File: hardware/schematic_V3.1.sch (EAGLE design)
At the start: 22 parts, among them J1 POWER_JACKPTH, J2 ARDUINONANO, J3 ICSP, J4 ICSP, J5 2.54mm, J6 2.54mm, J7 2.54mm, J8 2.54mm, J9 2.54mm, U1 L9110S_DRIVER

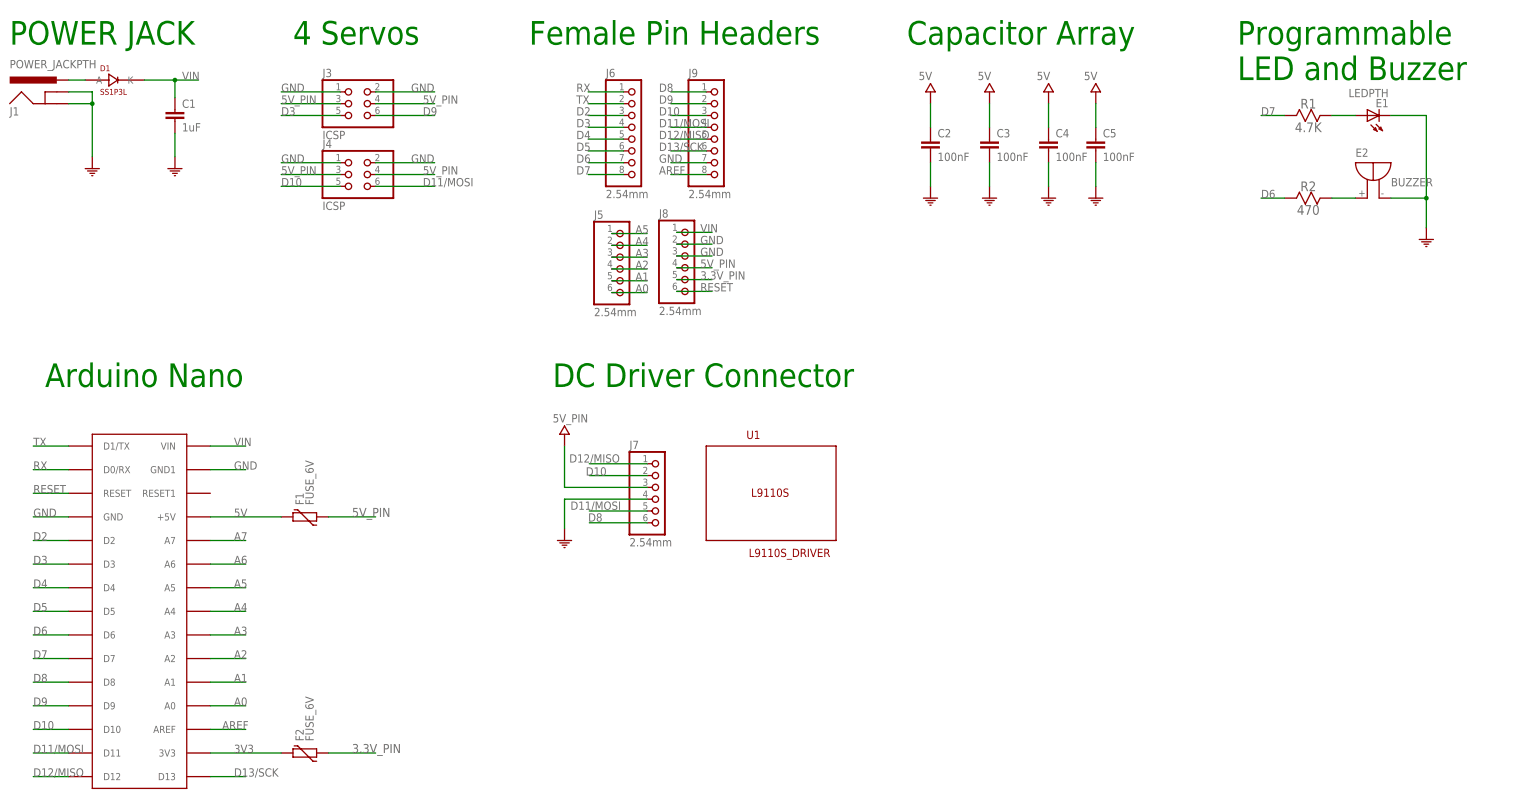
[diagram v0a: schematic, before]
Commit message: Finished routing and change the logo
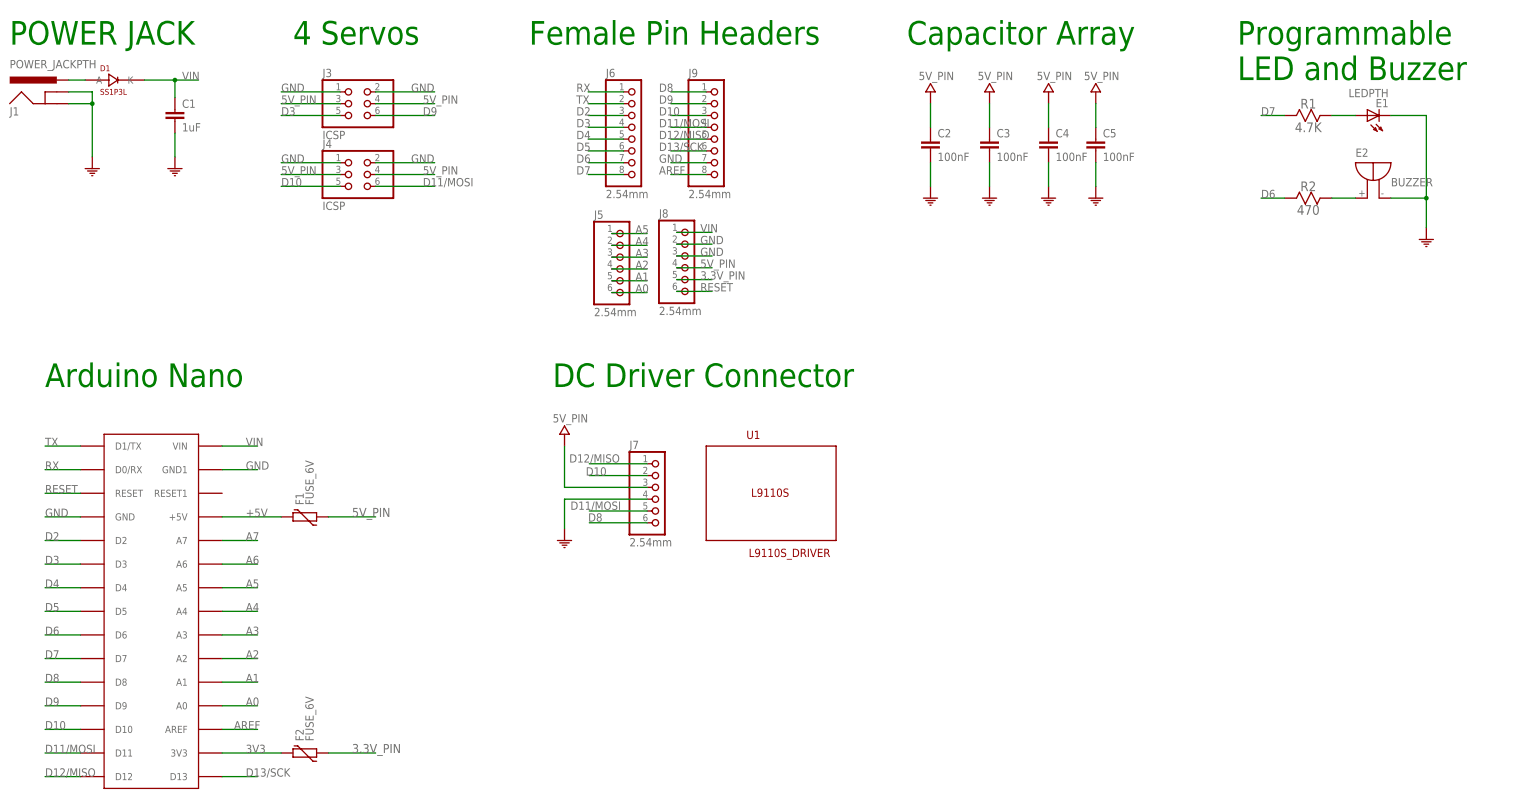
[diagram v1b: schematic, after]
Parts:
- removed J2: ARDUINONANO, barnabas_noggin_V4:ARDUINONANO
- added U$1: ARDUINONANO, barnabas_noggin_V4:ARDUINONANO
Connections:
- removed net 5V: C2.1, C3.1, C4.1, C5.1, F1.2, J2.+5V
- new net +5V: F1.2, U$1.+5V
- net 3V3: now also U$1.3V3; no longer J2.3V3
- net 5V_PIN: now also C2.1, C3.1, C4.1, C5.1
- net A0: now also U$1.A0; no longer J2.A0
- net A1: now also U$1.A1; no longer J2.A1
- net A2: now also U$1.A2; no longer J2.A2
- net A3: now also U$1.A3; no longer J2.A3
- net A4: now also U$1.A4; no longer J2.A4
- net A5: now also U$1.A5; no longer J2.A5
- net A6: now also U$1.A6; no longer J2.A6
- net A7: now also U$1.A7; no longer J2.A7
- net AREF: now also U$1.AREF; no longer J2.AREF
- net D10: now also U$1.D10; no longer J2.D10
- net D11/MOSI: now also U$1.D11; no longer J2.D11
- net D12/MISO: now also U$1.D12; no longer J2.D12
- net D13/SCK: now also U$1.D13; no longer J2.D13
- net D2: now also U$1.D2; no longer J2.D2
- net D3: now also U$1.D3; no longer J2.D3
- net D4: now also U$1.D4; no longer J2.D4
- net D5: now also U$1.D5; no longer J2.D5
- net D6: now also U$1.D6; no longer J2.D6
- net D7: now also U$1.D7; no longer J2.D7
- net D8: now also U$1.D8; no longer J2.D8
- net D9: now also U$1.D9; no longer J2.D9
- net GND: now also U$1.GND, U$1.GND1; no longer J2.GND, J2.GND1
- net RESET: now also U$1.RESET; no longer J2.RESET
- net RX: now also U$1.D0/RX; no longer J2.D0/RX
- net TX: now also U$1.D1/TX; no longer J2.D1/TX
- net VIN: now also U$1.VIN; no longer J2.VIN

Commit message: Moved the logo and generated BOM
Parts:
- F1, F2: PARTNO (none) -> MF-FSMF050X-2
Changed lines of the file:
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@@
 <part name="SYMBLE3" library="barnabas_noggin_V4" deviceset="5V_PIN" device=""/>
 <part name="SYMBLE4" library="barnabas_noggin_V4" deviceset="GND" device=""/>
-<part name="F1" library="barnabas_noggin_V4" deviceset="FUSE_6V" device=""/>
-<part name="F2" library="barnabas_noggin_V4" deviceset="FUSE_6V" device=""/>
+<part name="F1" library="barnabas_noggin_V4" deviceset="FUSE_6V" device="">
+<attribute name="PARTNO" value="MF-FSMF050X-2"/>
+</part>
+<part name="F2" library="barnabas_noggin_V4" deviceset="FUSE_6V" device="">
+<attribute name="PARTNO" value="MF-FSMF050X-2"/>
+</part>
 <part name="U$1" library="barnabas_noggin_V4" deviceset="ARDUINONANO" device=""/>
 <part name="SYMBLE5" library="barnabas_noggin_V4" deviceset="5V_PIN" device=""/>
@@
 <instance part="SYMBLE3" gate="G$1" x="106.68" y="40.64"/>
 <instance part="SYMBLE4" gate="G$1" x="106.68" y="17.78"/>
-<instance part="F1" gate="G$1" x="50.8" y="22.86" rot="R90"/>
-<instance part="F2" gate="G$1" x="50.8" y="-27.94" rot="R90"/>
+<instance part="F1" gate="G$1" x="50.8" y="22.86" rot="R90">
+<attribute name="PARTNO" x="50.8" y="22.86" size="1.778" layer="96" rot="R90" display="off"/>
+</instance>
+<instance part="F2" gate="G$1" x="50.8" y="-27.94" rot="R90">
+<attribute name="PARTNO" x="50.8" y="-27.94" size="1.778" layer="96" rot="R90" display="off"/>
+</instance>
 <instance part="U$1" gate="G$1" x="7.62" y="40.64"/>
 <instance part="SYMBLE5" gate="G$1" x="185.42" y="114.3"/>

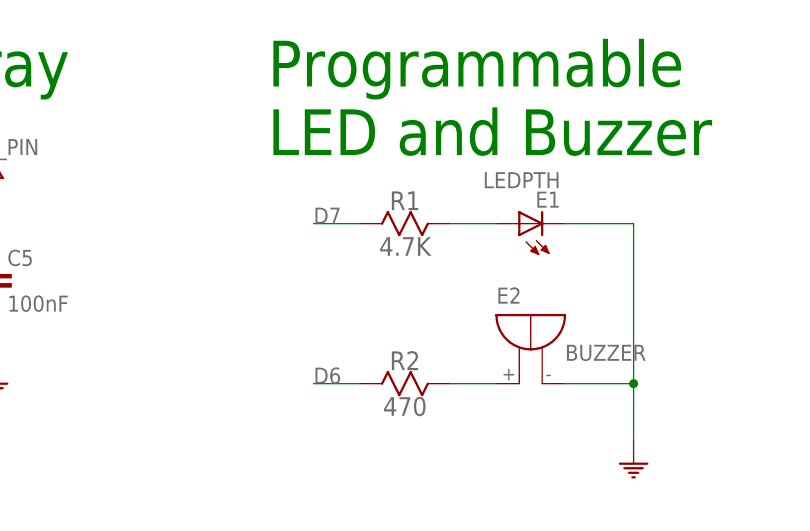
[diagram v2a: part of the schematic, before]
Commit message: change 4.7K resistor to 470 resistor
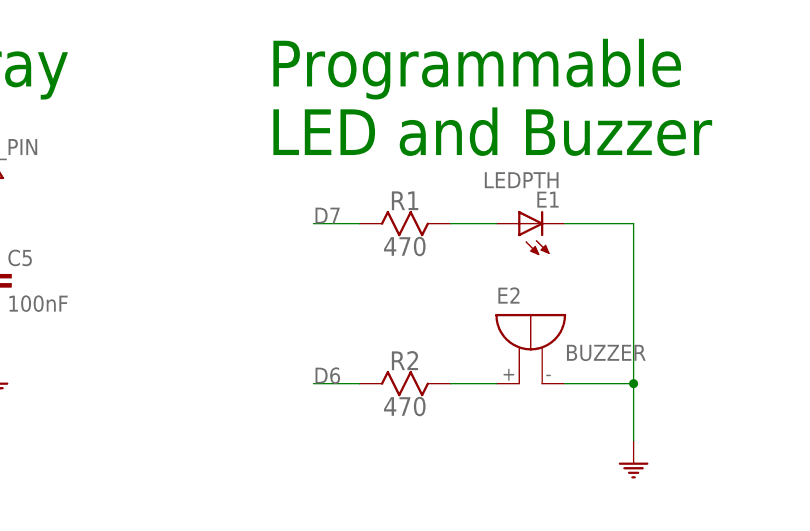
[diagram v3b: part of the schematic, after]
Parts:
- R1: value 4.7K -> 470
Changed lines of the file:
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@@
 </part>
 <part name="SYMBLE12" library="barnabas_noggin_V4" deviceset="GND" device=""/>
-<part name="R1" library="barnabas_noggin_V4" deviceset="RESISTOR" device="" value="4.7K"/>
+<part name="R1" library="barnabas_noggin_V4" deviceset="RESISTOR" device="" value="470"/>
 <part name="E1" library="barnabas_noggin_V4" deviceset="LEDPTH" device=""/>
 <part name="SYMBLE13" library="barnabas_noggin_V4" deviceset="GND" device=""/>
@@
 </sheet>
 </sheets>
+<errors>
+</errors>
 </schematic>
 </drawing>
